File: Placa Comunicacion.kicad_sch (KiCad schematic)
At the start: 35 parts, among them J1 Screw_Terminal_01x02, J3 Screw_Terminal_01x04, U5 AMS1117-3.3, U6 STM32F407VGTx, Y3 8Mhz

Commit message: Se estandariza algunos atributos: valores, librerias. Se actualiza pcb y se guarda.
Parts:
- C1: value 100nF 50V -> 100nF/50V
- C39: value 47uF 25V -> 47uF/25V
- C4, C6: value 30pF 50V -> 30pF/50V
- C40: value 4.7uF 25V -> 4u7F/25V
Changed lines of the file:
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@@
 			)
 		)
-		(property "Value" "30pF 50V"
+		(property "Value" "30pF/50V"
 			(at 171.45 87.63 90)
 			(effects
@@
 		(fields_autoplaced yes)
 		(property "Reference" "C39"
-			(at 100.33 263.525 0)
-			(effects
-				(font
-					(size 1.27 1.27)
-				)
-				(justify left)
-			)
-		)
-		(property "Value" "47uF 25V"
-			(at 100.33 266.065 0)
+			(at 100.33 262.8899 0)
+			(effects
+				(font
+					(size 1.27 1.27)
+				)
+				(justify left)
+			)
+		)
+		(property "Value" "47uF/25V"
+			(at 100.33 265.4299 0)
 			(effects
 				(font
@@
 			)
 		)
-		(property "Value" "100nF 50V"
+		(property "Value" "100nF/50V"
 			(at 182.88 41.91 0)
 			(effects
@@
 			)
 		)
-		(property "Value" "30pF 50V"
+		(property "Value" "30pF/50V"
 			(at 171.45 64.77 90)
 			(effects
@@
 		(fields_autoplaced yes)
 		(property "Reference" "C40"
-			(at 127 262.89 0)
-			(effects
-				(font
-					(size 1.27 1.27)
-				)
-				(justify left)
-			)
-		)
-		(property "Value" "4.7uF 25V"
-			(at 127 265.43 0)
-			(effects
-				(font
+			(at 127 262.8899 0)
+			(effects
+				(font
+					(size 1.27 1.27)
+				)
+				(justify left)
+			)
+		)
+		(property "Value" "4u7F/25V"
+			(at 127 265.4299 0)
+			(effects
+				(font

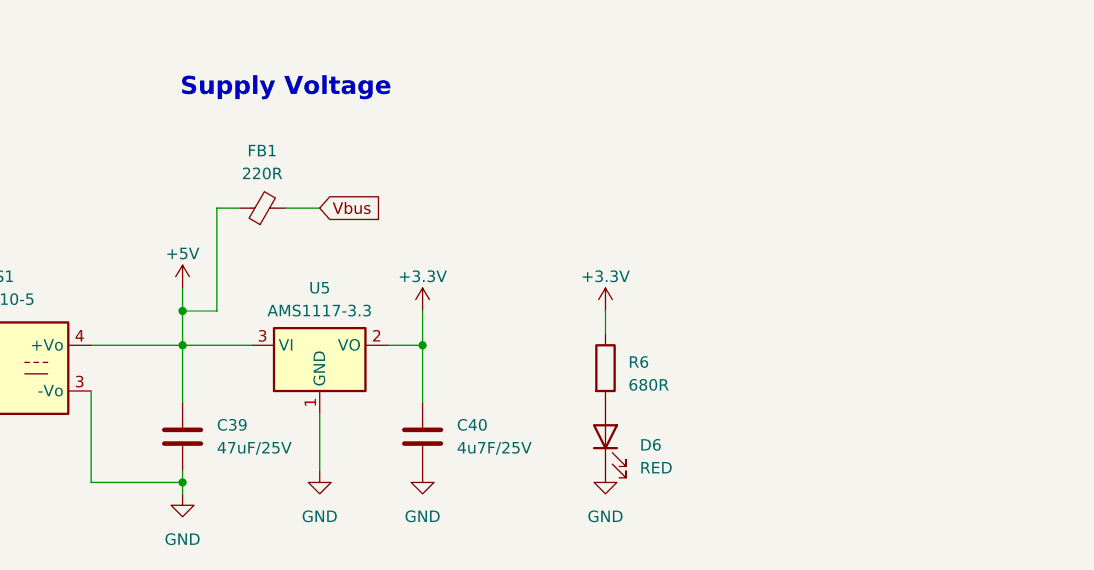
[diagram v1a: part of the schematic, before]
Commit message: Se estandariza losc omponentes, se cambian algunos valores para evitar gastos adicionales. Se termina y comprueb el part list para jlcpcb
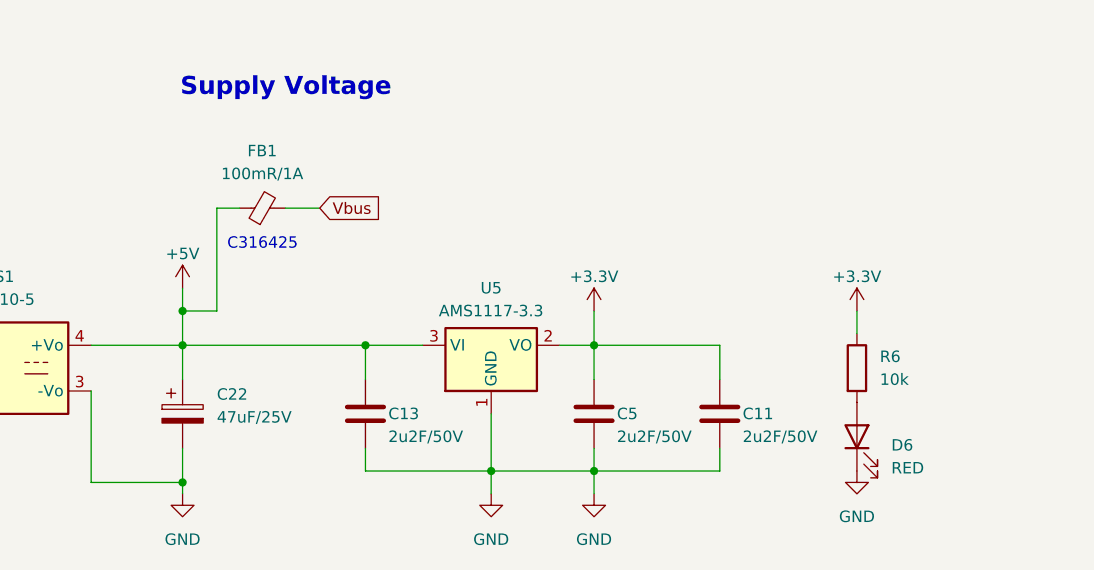
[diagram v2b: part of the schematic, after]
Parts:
- removed C39: 47uF/25V, 1-Capacitor:C_1206_3216Metric, symbol 1-Capacitor:C_1206
- removed C40: 4u7F/25V, 1-Capacitor:C_1206_3216Metric, symbol 1-Capacitor:C_1206
- added C11, C13, C5: 2u2F/50V, Capacitor_SMD:C_0805_2012Metric, symbol 1-Capacitor:C_0805
- added C22: 47uF/25V, Capacitor_THT:CP_Radial_D5.0mm_P2.50mm, symbol Device:C_Polarized
- FB1: value 220R -> 100mR/1A; footprint 1-Resistor:R_0805_2012Metric -> Inductor_SMD:L_0805_2012Metric
- R6: value 680R -> 10k
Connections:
- net +3.3V: now also C11.1, C5.1
- net +5V: now also C13.1, C22.1
- net GND: now also C11.2, C13.2, C22.2, C5.2
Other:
- note added: "C316425"
- moved on the sheet: D6, R6, U5

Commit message: Se añade led status y eeprom externa. Se actutliza y añade serigrafía a la pcb, se escoge uC de menos flash debido a la escasez del uC planeado, sin embargo, funcionará a recomendacion del programador. Se revisa en jlcpcb y se espera su envío
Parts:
- added C79: 100nF/50V, 1-Capacitor:C_0603_1608Metric, symbol 1-Capacitor:C_0603
- added D1: RED, 1-Led:LED_0805, symbol 1-Led:LED_0805
- added R129, R130, R5: 2k2, Resistor_SMD:R_0603_1608Metric, symbol 1-Resistor:R_0603
- added U23: 24xx256, Package_SO:SO-8_3.9x4.9mm_P1.27mm, symbol 1-IC-General:24xx256
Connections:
- net +3.3V: now also C79.1, R129.2, R130.2, U23.8 (VCC)
- net GND: now also C79.2, D1.1 (K), U23.1 (A0), U23.2 (A1), U23.3 (A2), U23.4 (GND), U23.7 (WP)
- net LED_STATUS: now reaches U6.63 (PC6)
- net LED_STATUS: now also R5.1
- net MCU_I2C3_SDA: now reaches U6.66 (PC9)
- net MCU_I2C3_SDA: now also R129.1, U23.5 (SDA)
- net MCU_I2C3_SCL: now reaches U6.67 (PA8)
- net MCU_I2C3_SCL: now also R130.1, U23.6 (SCL)
- new net: D1.2 (A), R5.2
- no-connect marks 57 -> 56
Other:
- note added: "Address = 000"
- note added: "WP=0 ->Normal Operation"
